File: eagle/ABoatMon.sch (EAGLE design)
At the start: 29 parts, among them J1 5V, J2 GND, J3 GND, J4 5V, X1 MKDSN1,5/3-5,08, X6 MKDSN1,5/3-5,08

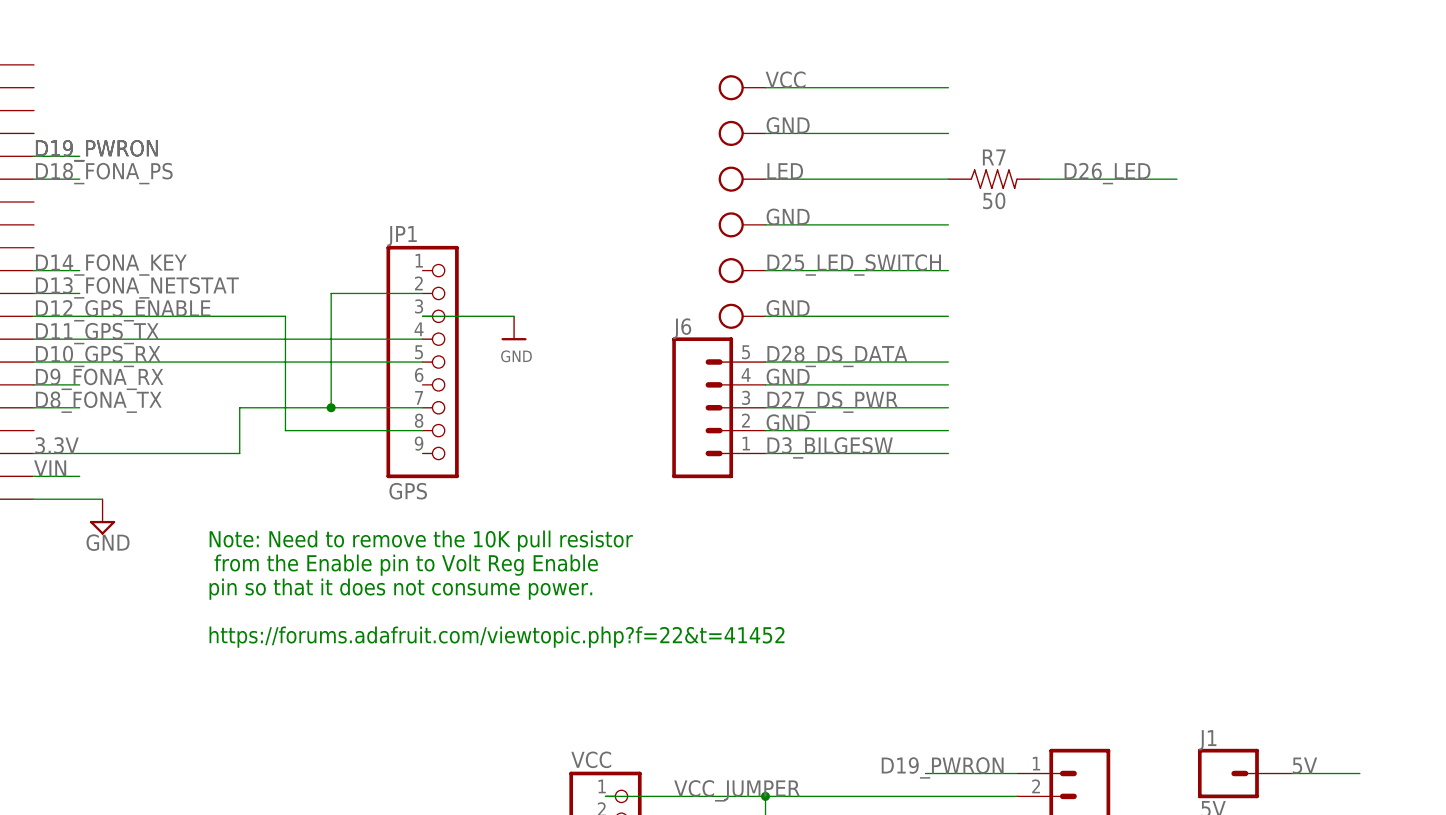
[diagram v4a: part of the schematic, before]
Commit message: bigger JST, added 4.7K
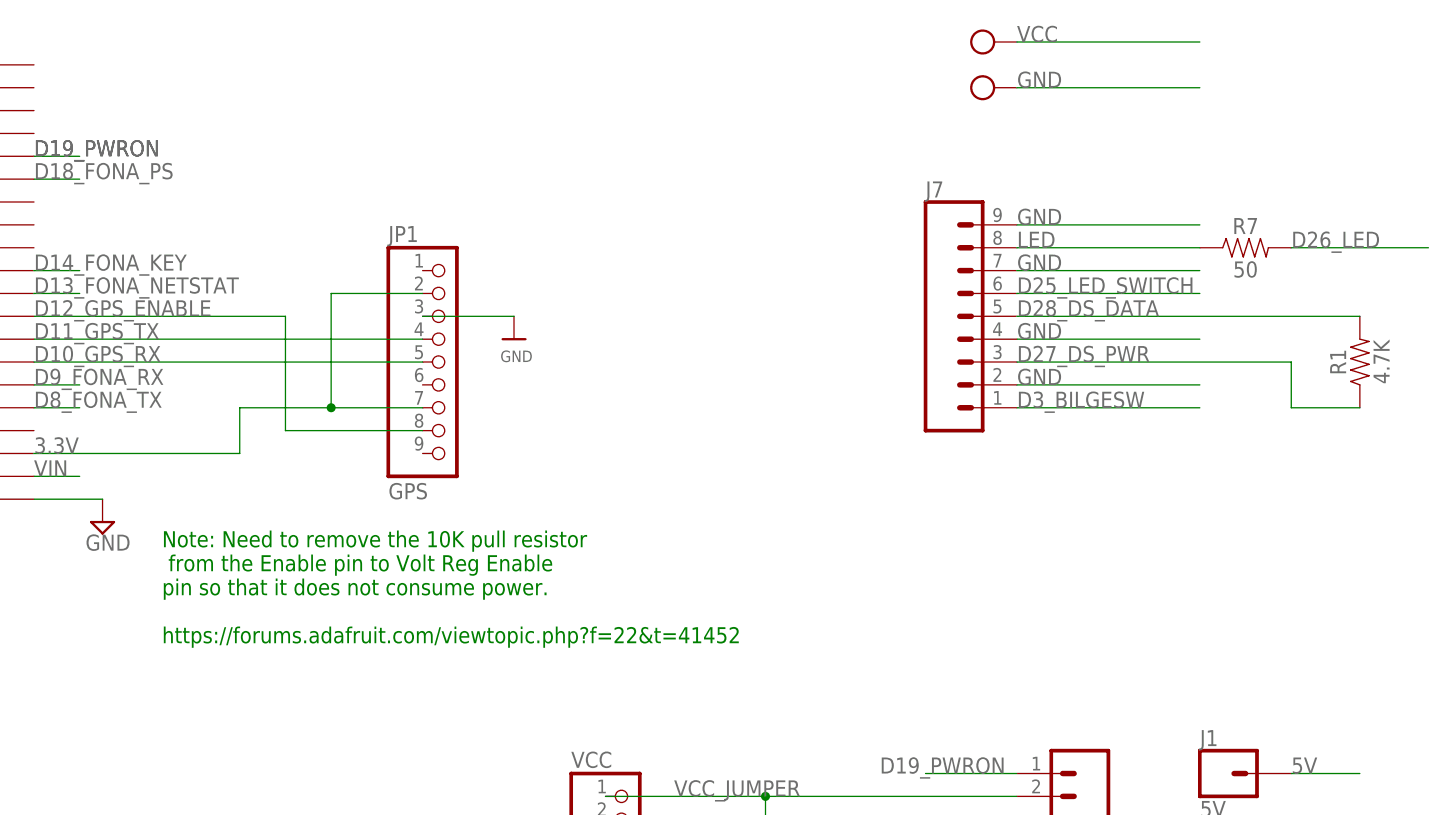
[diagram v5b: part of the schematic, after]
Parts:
- removed J6: (no value), SparkFun-Connectors:CONN_05JST
- removed X6: MKDSN1,5/3-5,08, con-phoenix-508:MKDSN1,5/3-5,08
- added J7: (no value), SparkFun-Connectors:CONN_09
- added R1: 4.7K, SparkFun-Resistors:1KOHM-HORIZ-1/4W-1%
- X1: value MKDSN1,5/3-5,08 -> MKDSN1,5/2-5,08; device con-phoenix-508:MKDSN1,5/3-5,08 -> con-phoenix-508:MKDSN1,5/2-5,08
- renumbered U$6 to GND
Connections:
- net D25_LED_SWITCH: now also J7.6; no longer X1-2.KL
- net D27_DS_PWR: now also J7.3, R1.1; no longer J6.3
- net D28_DS_DATA: now also J7.5, R1.2; no longer J6.5
- net D3_BILGESW: now also J7.1; no longer J6.1
- net GND: now also J7.2, J7.4, J7.7, J7.9, X1-2.KL; no longer J6.2, J6.4, X1-1.KL, X1-3.KL, X6-2.KL
- net LED: now also J7.8; no longer X6-3.KL
- net VCC: now also X1-1.KL; no longer X6-1.KL
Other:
- moved on the sheet: R7

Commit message: DRC, ERC pass
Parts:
- renumbered J7 to JST
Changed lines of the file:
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@@
 <part name="U$7" library="microbuilder" deviceset="MOUNTINGHOLE" device="2.5"/>
 <part name="U$8" library="microbuilder" deviceset="MOUNTINGHOLE" device="2.5"/>
-<part name="J7" library="SparkFun-Connectors" library_urn="urn:adsk.eagle:library:513" deviceset="CONN_09" device="" package3d_urn="urn:adsk.eagle:package:38153/1"/>
+<part name="JST" library="SparkFun-Connectors" library_urn="urn:adsk.eagle:library:513" deviceset="CONN_09" device="" package3d_urn="urn:adsk.eagle:package:38153/1"/>
 <part name="X1" library="con-phoenix-508" library_urn="urn:adsk.eagle:library:176" deviceset="MKDSN1,5/2-5,08" device="" package3d_urn="urn:adsk.eagle:package:9630/1"/>
 <part name="R1" library="SparkFun-Resistors" deviceset="1KOHM" device="-HORIZ-1/4W-1%" value="4.7K"/>
@@
 <instance part="U$7" gate="G$1" x="81.28" y="12.7" smashed="yes"/>
 <instance part="U$8" gate="G$1" x="88.9" y="12.7" smashed="yes"/>
-<instance part="J7" gate="G$1" x="205.74" y="134.62" smashed="yes">
+<instance part="JST" gate="G$1" x="205.74" y="134.62" smashed="yes">
 <attribute name="VALUE" x="205.74" y="119.634" size="1.778" layer="96" font="vector"/>
 <attribute name="NAME" x="205.74" y="147.828" size="1.778" layer="95" font="vector"/>
@@
 <wire x1="215.9" y1="139.7" x2="236.22" y2="139.7" width="0.1524" layer="91"/>
 <label x="215.9" y="139.7" size="1.778" layer="95"/>
-<pinref part="J7" gate="G$1" pin="7"/>
+<pinref part="JST" gate="G$1" pin="7"/>
 </segment>
 <segment>
 <wire x1="215.9" y1="127" x2="236.22" y2="127" width="0.1524" layer="91"/>
 <label x="215.9" y="127" size="1.778" layer="95"/>
-<pinref part="J7" gate="G$1" pin="2"/>
+<pinref part="JST" gate="G$1" pin="2"/>
 </segment>
 <segment>
 <wire x1="215.9" y1="132.08" x2="236.22" y2="132.08" width="0.1524" layer="91"/>
 <label x="215.9" y="132.08" size="1.778" layer="95"/>
-<pinref part="J7" gate="G$1" pin="4"/>
-</segment>
-<segment>
-<pinref part="J7" gate="G$1" pin="9"/>
+<pinref part="JST" gate="G$1" pin="4"/>
+</segment>
+<segment>
+<pinref part="JST" gate="G$1" pin="9"/>
 <wire x1="215.9" y1="144.78" x2="236.22" y2="144.78" width="0.1524" layer="91"/>
 <label x="215.9" y="144.78" size="1.778" layer="95"/>
@@
 </segment>
 <segment>
-<pinref part="J7" gate="G$1" pin="6"/>
+<pinref part="JST" gate="G$1" pin="6"/>
 <wire x1="215.9" y1="137.16" x2="236.22" y2="137.16" width="0.1524" layer="91"/>
 <label x="215.9" y="137.16" size="1.778" layer="95"/>
@@
 <wire x1="215.9" y1="124.46" x2="236.22" y2="124.46" width="0.1524" layer="91"/>
 <label x="215.9" y="124.46" size="1.778" layer="95"/>
-<pinref part="J7" gate="G$1" pin="1"/>
+<pinref part="JST" gate="G$1" pin="1"/>
 </segment>
 </net>
@@
 <wire x1="215.9" y1="134.62" x2="254" y2="134.62" width="0.1524" layer="91"/>
 <label x="215.9" y="134.62" size="1.778" layer="95"/>
-<pinref part="J7" gate="G$1" pin="5"/>
+<pinref part="JST" gate="G$1" pin="5"/>
 <pinref part="R1" gate="G$1" pin="2"/>
 </segment>
@@
 <wire x1="215.9" y1="129.54" x2="246.38" y2="129.54" width="0.1524" layer="91"/>
 <label x="215.9" y="129.54" size="1.778" layer="95"/>
-<pinref part="J7" gate="G$1" pin="3"/>
+<pinref part="JST" gate="G$1" pin="3"/>
 <wire x1="246.38" y1="129.54" x2="246.38" y2="124.46" width="0.1524" layer="91"/>
 <pinref part="R1" gate="G$1" pin="1"/>
@@
 <net name="LED" class="0">
 <segment>
-<pinref part="J7" gate="G$1" pin="8"/>
+<pinref part="JST" gate="G$1" pin="8"/>
 <pinref part="R7" gate="G$1" pin="1"/>
 <wire x1="215.9" y1="142.24" x2="236.22" y2="142.24" width="0.1524" layer="91"/>
